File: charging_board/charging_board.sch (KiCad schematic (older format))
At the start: 63 parts

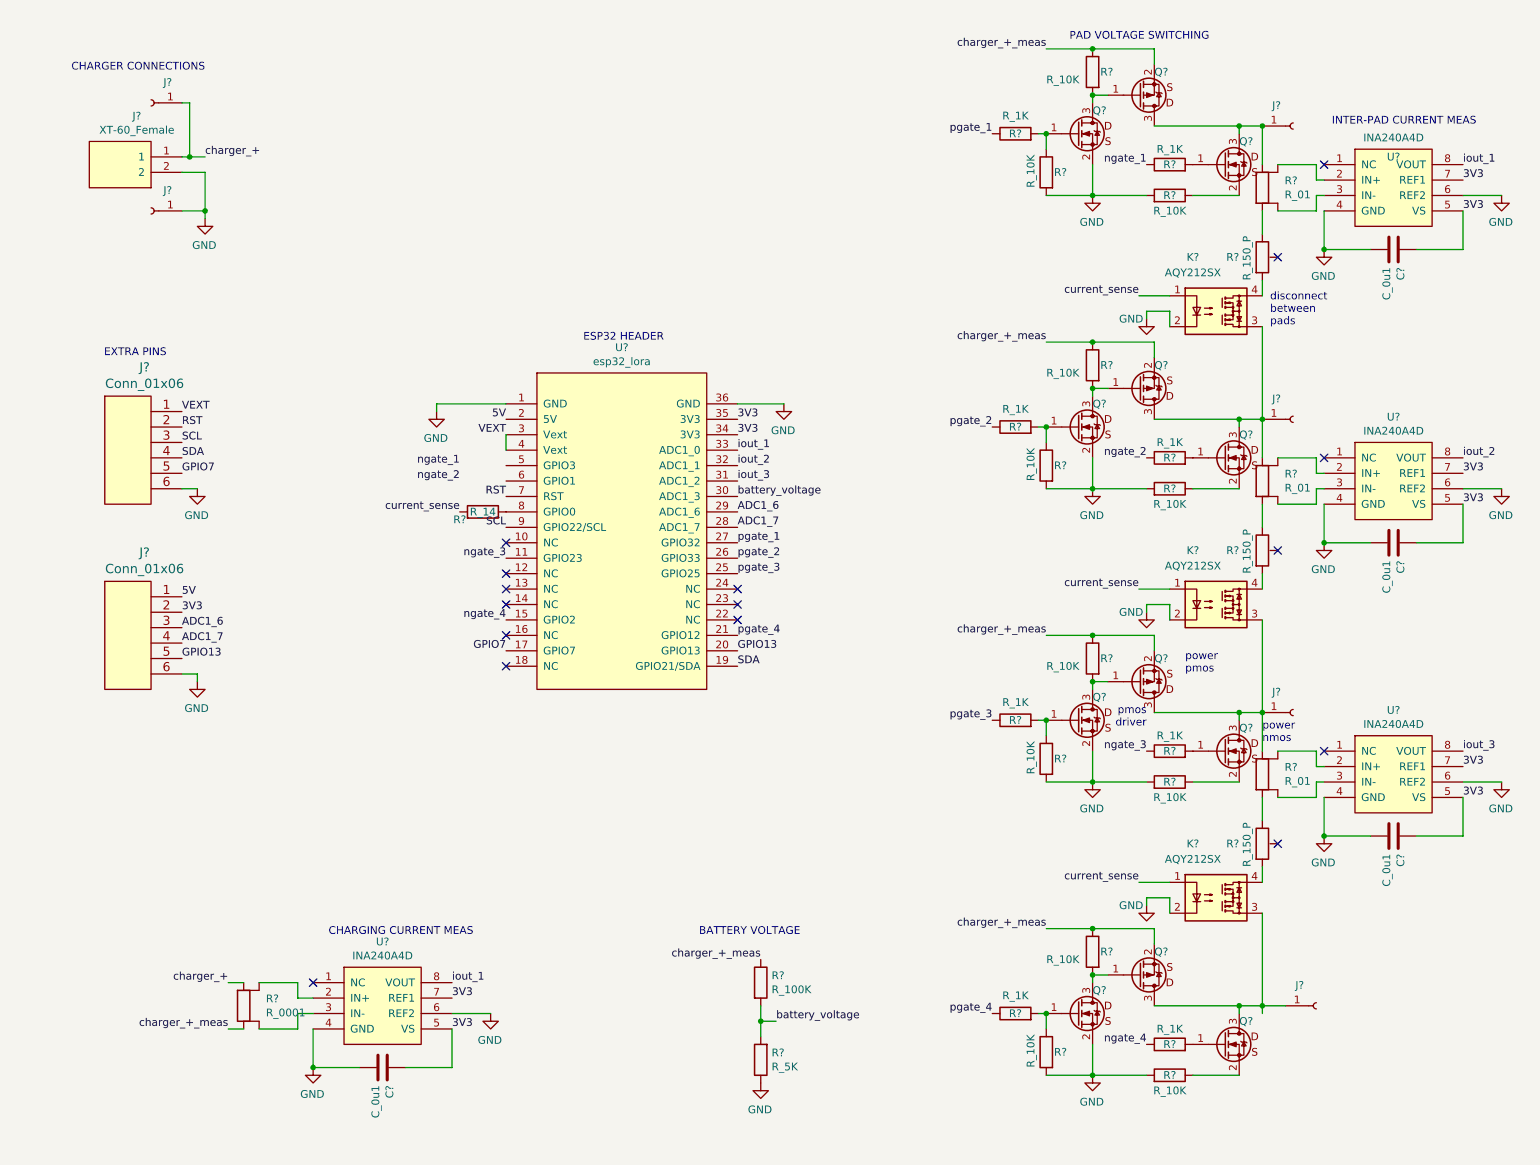
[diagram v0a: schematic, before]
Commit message: finalized charging board design
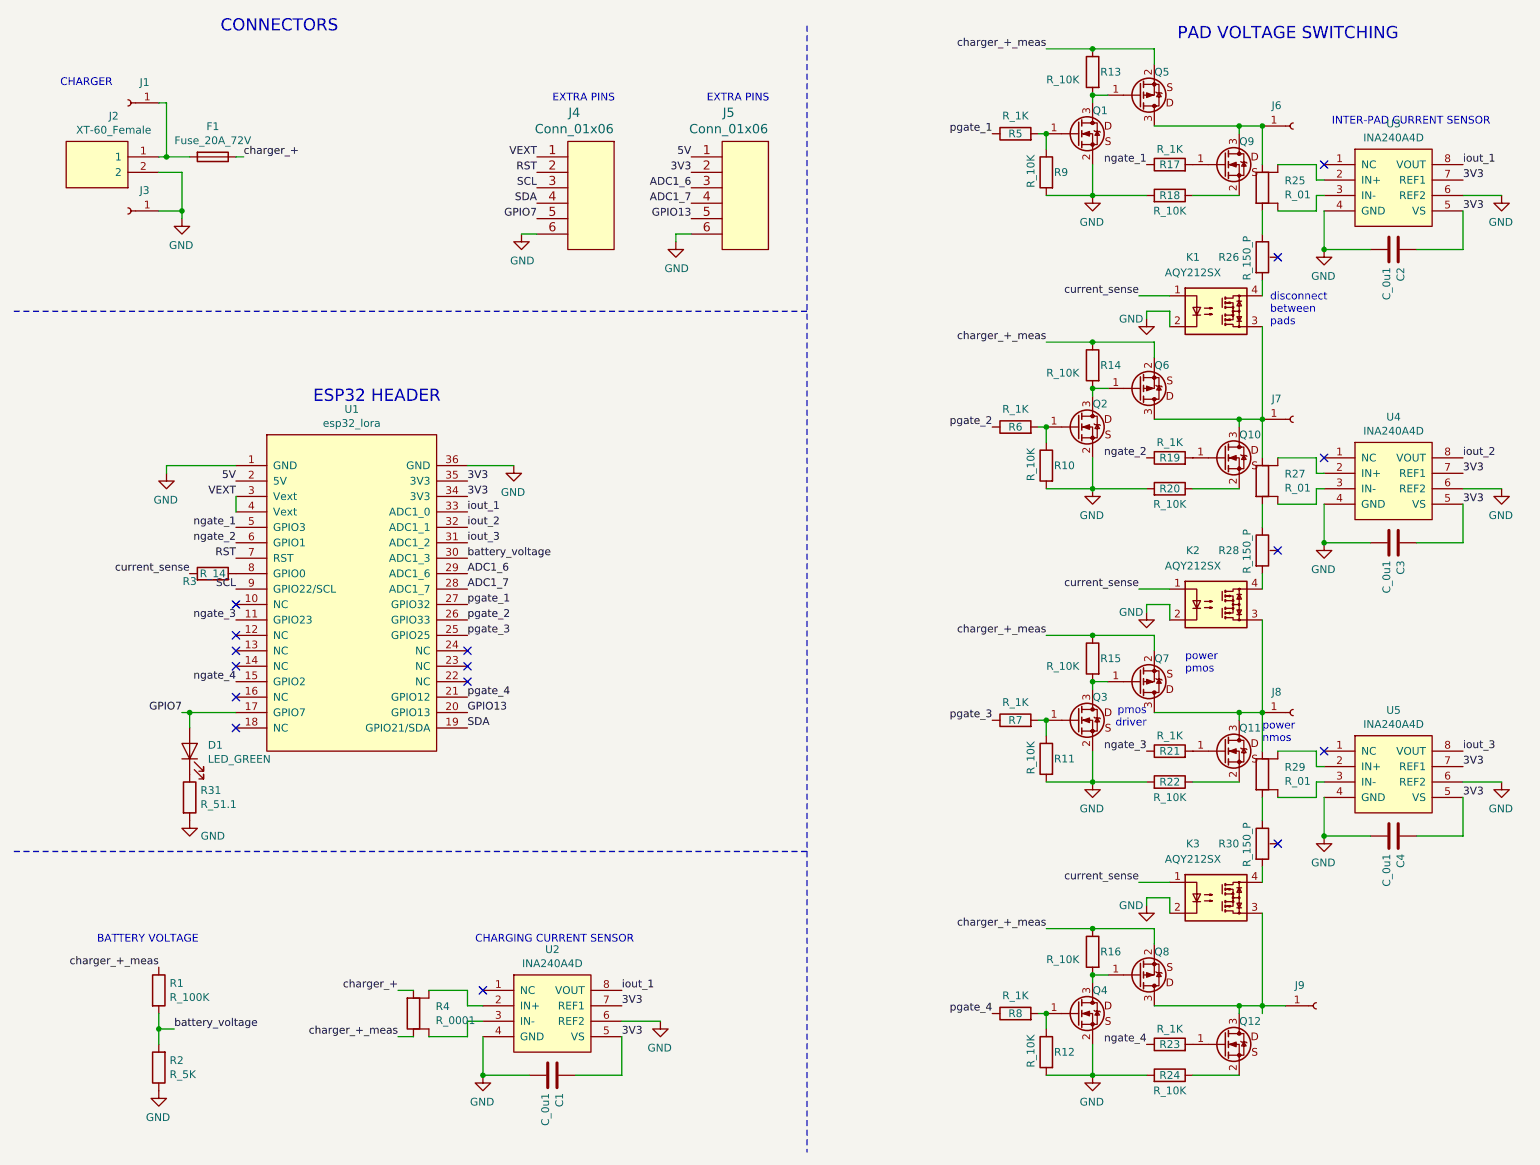
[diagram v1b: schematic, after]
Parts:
- removed U? (x4): INA240A4D, personal:SOIC-8_3.9x4.9mm_Pitch1.27mm, symbol personal:INA240A4D
- added D1: LED_GREEN, LEDs:LED_0603_HandSoldering, symbol personal:LED_GREEN
- added F1: Fuse_20A_72V, personal:0697H9200-01, symbol personal:Fuse_20A_72V
- added R31: R_51.1, personal:R_0805, symbol personal:R_51.1
- added U2, U3, U4, U5: INA240A4D, personal:SOIC-8_3.9x4.9mm_Pitch1.27mm, symbol personal:INA240A4D
- gave numbers to parts that had none: 59
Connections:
- net 3V3: now also U2.5 (VS), U2.7 (REF1), U3.5 (VS), U3.7 (REF1), U4.5 (VS), U4.7 (REF1), U5.5 (VS), U5.7 (REF1)
- net GND: now also R31.2, U2.4 (GND), U2.6 (REF2), U3.4 (GND), U3.6 (REF2), U4.4 (GND), U4.6 (REF2), U5.4 (GND), U5.6 (REF2)
- net GPIO7: now also D1.2 (A)
- net charger_+: now also F1.1; no longer J1.1 (Pin_1), J2.1
- net iout_1: now also U2.8 (VOUT), U3.8 (VOUT)
- net iout_2: now also U4.8 (VOUT)
- net iout_3: now also U5.8 (VOUT)
- net ngate_1: now also U1.5 (GPIO3)
- net ngate_2: now also U1.6 (GPIO1)
- net at R25.3: now also U3.2 (IN+)
- net at R25.4: now also U3.3 (IN-)
- net at R4.4: now also U2.2 (IN+)
- net at R4.3: now also U2.3 (IN-)
- net at R27.3: now also U4.2 (IN+)
- net at R27.4: now also U4.3 (IN-)
- net at R29.3: now also U5.2 (IN+)
- net at R29.4: now also U5.3 (IN-)
- new net: F1.2, J1.1 (Pin_1), J2.1
- new net: D1.1 (K), R31.1
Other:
- note added: "CHARGER"
- note added: "CHARGING CURRENT SENSOR\n"
- note added: "CONNECTORS"
- note added: "INTER-PAD CURRENT SENSOR\n"
- note removed: "CHARGER CONNECTIONS"
- note removed: "CHARGING CURRENT MEAS\n"
- note removed: "INTER-PAD CURRENT MEAS\n"
- moved on the sheet: C1, J1, J2, J3, J4, J5, R1, R2, R3, R4, U1
